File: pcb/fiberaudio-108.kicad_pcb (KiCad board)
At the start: 2 copper layers, 0 parts

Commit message: Add schematic, custom components and initial layout
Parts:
- added C1: 10nF, Capacitor_SMD:C_0805_2012Metric, F.Cu at (68.6, 42.2)
- added C2: 100nF, Capacitor_SMD:C_0805_2012Metric, F.Cu at (73.7, 41.9)
- added C3: 4.7uF, Capacitor_Tantalum_SMD:CP_EIA-3216-18_Kemet-A, F.Cu at (76.2, 42.0)
- added C4: 4.7uF, Capacitor_SMD:C_0805_2012Metric, F.Cu at (78.7, 58.4)
- added C5: 20pF, Capacitor_SMD:C_0805_2012Metric, F.Cu at (94.0, 58.4)
- added C6: 20pF, Capacitor_SMD:C_0805_2012Metric, F.Cu at (86.4, 58.4)
- added C7: 100nF, Capacitor_SMD:C_0805_2012Metric, F.Cu at (81.3, 58.4)
- added C8: 4.7uF, Capacitor_SMD:C_0805_2012Metric, F.Cu at (86.4, 41.9)
- added C9: 100nF, Capacitor_SMD:C_0805_2012Metric, F.Cu at (107.6, 45.7)
- added FB1: 33R@100MHz, Inductor_SMD:L_0805_2012Metric, F.Cu at (71.1, 45.7)
- added J1: USB_B_Mini, Connector_USB:USB_Mini-B_Lumberg_2486_01_Horizontal, F.Cu at (62.2, 49.5)
- added J2: PLT133_T10W, custom:PLT133_T10W, F.Cu at (115.6, 49.5)
- added LD1: rd, LED_THT:LED_D3.0mm_FlatTop, F.Cu at (100.3, 49.5)
- added Q1: DMG2301L, Package_TO_SOT_SMD:SOT-23, F.Cu at (108.0, 49.5)
- added R1: 270, Resistor_SMD:R_0805_2012Metric, F.Cu at (101.6, 53.3)
- added R2: 560, Resistor_SMD:R_0805_2012Metric, F.Cu at (108.0, 53.3)
- added SW1: MUTE, Button_Switch_SMD:SW_SPST_B3S-1000, F.Cu at (94.0, 49.5)
- added U1: STF202-22T1, Package_SO:TSOP-6_1.65x3.05mm_P0.95mm, F.Cu at (71.1, 49.5)
- added U2: AT93C46E, Package_SO:SOIC-8_3.9x4.9mm_P1.27mm, F.Cu at (71.1, 55.9)
- added U3: CM108AH, Package_QFP:LQFP-48_7x7mm_P0.5mm, F.Cu at (82.5, 49.5)
- added Y1: 12MHz, Crystal:Crystal_SMD_3225-4Pin_3.2x2.5mm, F.Cu at (90.2, 58.4)

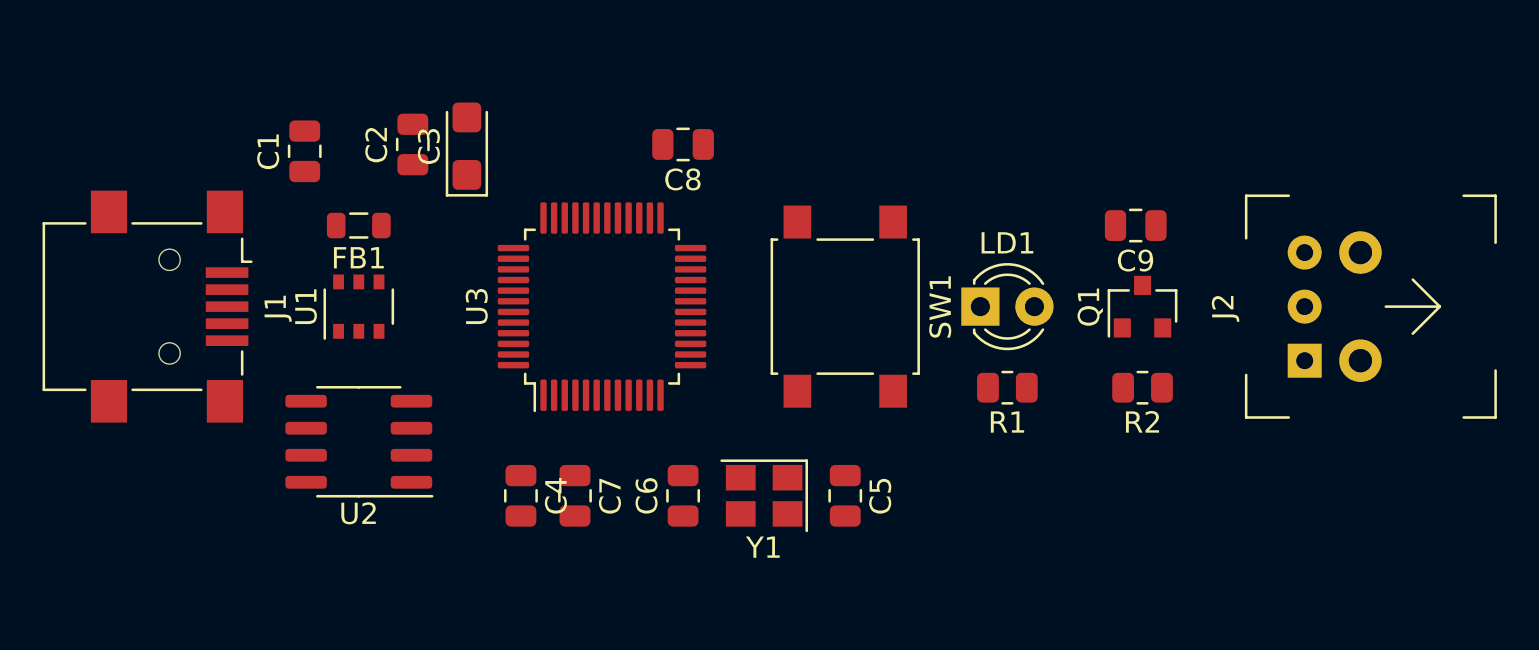
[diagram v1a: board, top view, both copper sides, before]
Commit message: Add initial routed layout
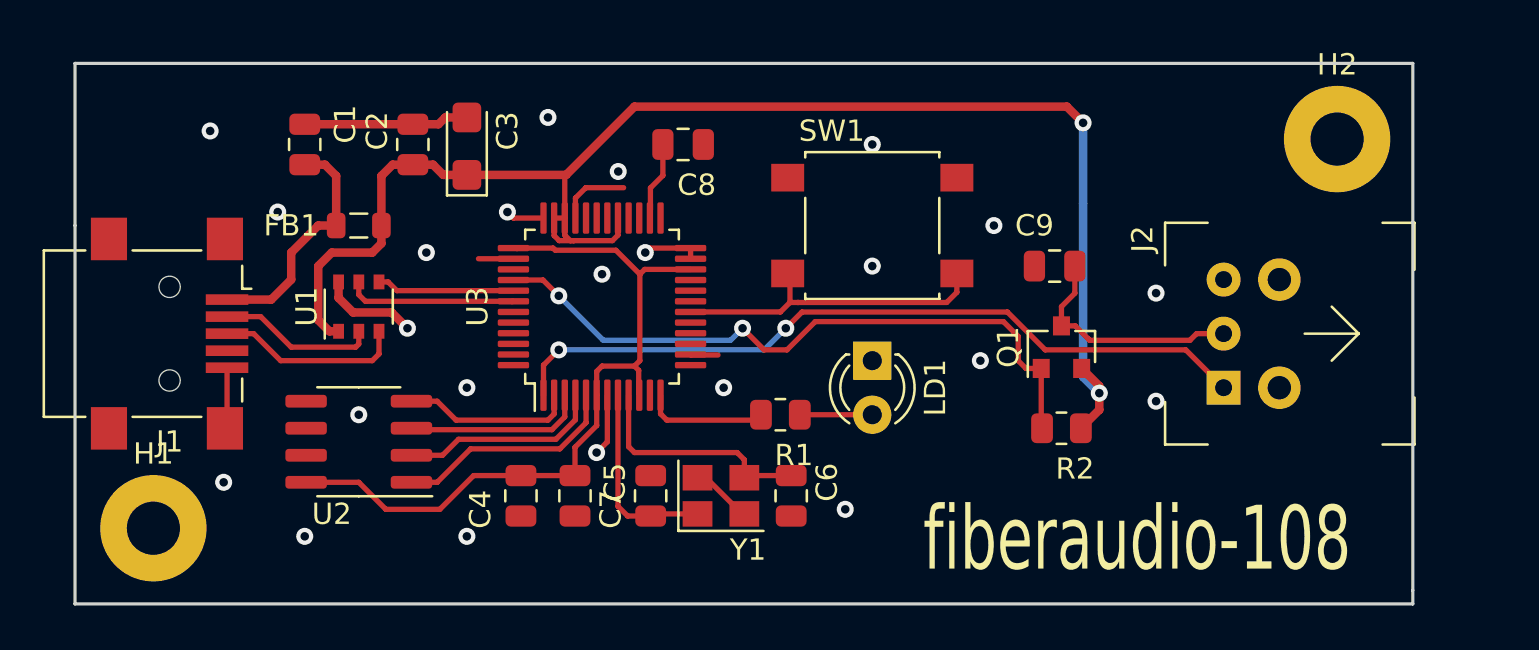
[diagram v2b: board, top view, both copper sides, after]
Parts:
- added H1: MountingHole_Pad, MountingHole:MountingHole_2.5mm_Pad, F.Cu at (61.5, 59.9)
- added H2: MountingHole_Pad, MountingHole:MountingHole_2.5mm_Pad, F.Cu at (117.1, 41.7)
- moved R1 10.7 mm to (90.9, 54.6)
- moved C5 9.14 mm to (84.8, 58.4), turned to 90 degrees
- moved LD1 5.68 mm to (95.2, 52.1), turned to 270 degrees
- moved C6 5.08 mm to (91.4, 58.4), turned to 270 degrees
- moved C9 4.26 mm to (103.8, 47.6)
- moved Q1 4.26 mm to (104.1, 51.4)
- moved R2 4.26 mm to (104.1, 55.2)
- moved SW1 4.02 mm to (95.2, 45.7), turned to 0 degrees
- moved J2 4.02 mm to (111.8, 50.8)
- moved Y1 2.03 mm to (88.1, 58.4), turned to 0 degrees
- moved J1 1.27 mm to (62.2, 50.8)
- moved C1 0.32 mm to (68.6, 41.9)
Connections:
- U3 pad 6: Net-(U3-Pad6) -> +3V3
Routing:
- net +5V: track 0.21 -> 70.6 mm, vias 0 -> 2
- net +3V3: track 0.00 -> 36.0 mm
- net /SPDIF_MOD: track 0.00 -> 35.9 mm, vias 0 -> 2
- net GND: track 0.00 -> 31.9 mm, vias 0 -> 23
- net /SPDIF_PWDN: track 0.00 -> 31.6 mm, vias 0 -> 2
- net /MUTE: track 0.00 -> 15.2 mm
- net /EECS: track 0.00 -> 11.5 mm
- net /VBUS: track 0.00 -> 11.3 mm
- net Net-(C9-Pad1): track 0.00 -> 11.1 mm
- net Net-(C6-Pad1): track 0.00 -> 10.7 mm
- net /EESK: track 0.00 -> 9.55 mm
- net Net-(C5-Pad1): track 0.00 -> 9.19 mm
- net /USBDP: track 0.00 -> 8.86 mm
- net /EEMOSI: track 0.00 -> 8.50 mm
- net /EEMISO: track 0.00 -> 8.07 mm
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- added copper zone on B.Cu, net GND
- added copper zone on F.Cu, net GND
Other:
- board outline added: 62.9 x 25.4 mm
- board text added: "fiberaudio-108"

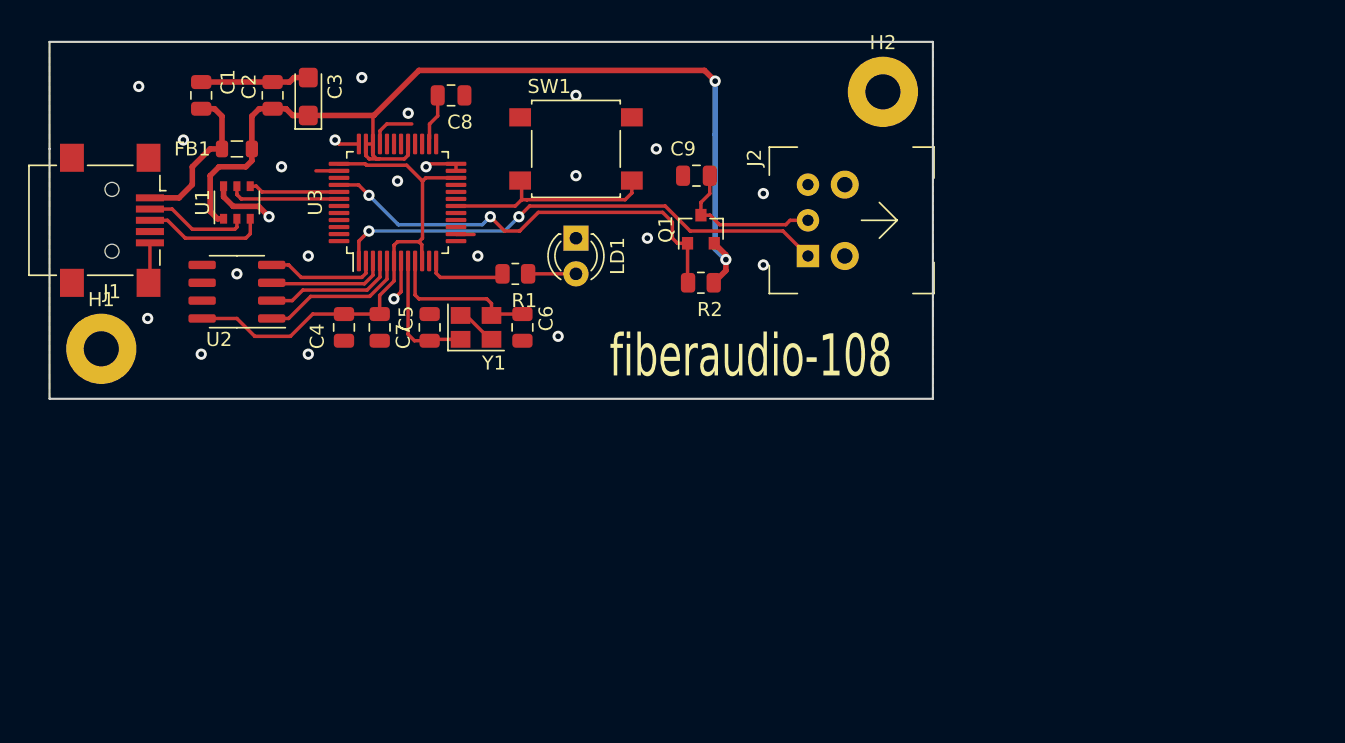
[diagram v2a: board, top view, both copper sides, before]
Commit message: Redesign for automated assembly
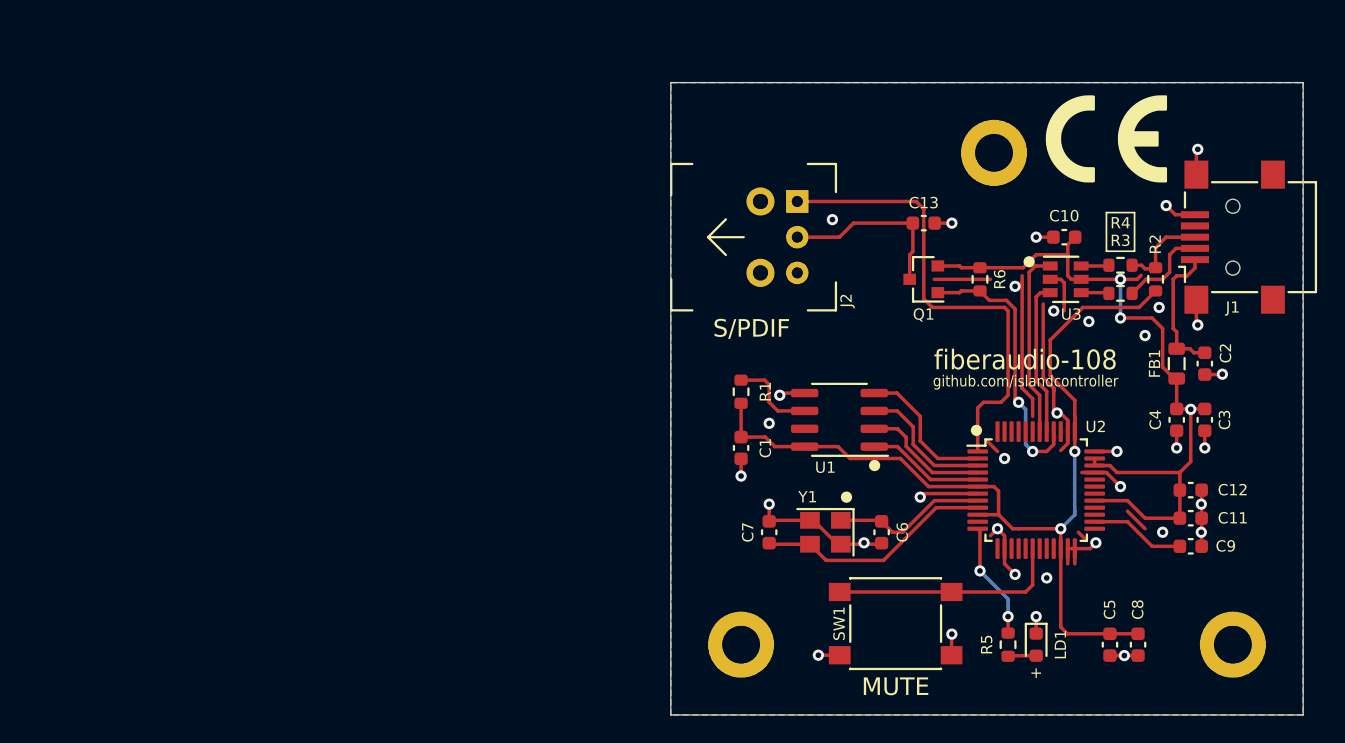
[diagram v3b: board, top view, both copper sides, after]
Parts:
- added C10: 100nF, Capacitor_SMD:C_0603_1608Metric, F.Cu at (130.0, 52.0)
- added C11: 100nF, Capacitor_SMD:C_0603_1608Metric, F.Cu at (139.0, 72.0)
- added C12: 100nF, Capacitor_SMD:C_0603_1608Metric, F.Cu at (139.0, 70.0)
- added C13: 100nF, Capacitor_SMD:C_0603_1608Metric, F.Cu at (120.0, 51.0)
- added H3: MountingHole_Pad, MountingHole:MountingHole_2.7mm_M2.5_DIN965_Pad, F.Cu at (125.0, 46.0)
- added R3: 22, Resistor_SMD:R_0603_1608Metric, F.Cu at (134.0, 56.0)
- added R4: 22, Resistor_SMD:R_0603_1608Metric, F.Cu at (134.0, 54.0)
- added R5: 330, Resistor_SMD:R_0603_1608Metric, F.Cu at (126.0, 81.0)
- added R6: 560, Resistor_SMD:R_0603_1608Metric, F.Cu at (124.0, 55.0)
- added REF**: CE-Logo_8.5x6mm_SilkScreen, Symbol:CE-Logo_8.5x6mm_SilkScreen, F.Cu at (133.0, 45.0)
- C1: value 10nF -> 100nF; footprint Capacitor_SMD:C_0805_2012Metric -> Capacitor_SMD:C_0603_1608Metric
- C2: value 100nF -> 10nF; footprint Capacitor_SMD:C_0805_2012Metric -> Capacitor_SMD:C_0603_1608Metric
- C3: value 4.7uF -> 100nF; footprint Capacitor_Tantalum_SMD:CP_EIA-3216-18_Kemet-A -> Capacitor_SMD:C_0603_1608Metric
- C4, C6: footprint Capacitor_SMD:C_0805_2012Metric -> Capacitor_SMD:C_0603_1608Metric
- C5: value 20pF -> 4.7uF; footprint Capacitor_SMD:C_0805_2012Metric -> Capacitor_SMD:C_0603_1608Metric
- C7: value 100nF -> 20pF; footprint Capacitor_SMD:C_0805_2012Metric -> Capacitor_SMD:C_0603_1608Metric
- C8: value 4.7uF -> 100nF; footprint Capacitor_SMD:C_0805_2012Metric -> Capacitor_SMD:C_0603_1608Metric
- C9: value 100nF -> 4.7uF; footprint Capacitor_SMD:C_0805_2012Metric -> Capacitor_SMD:C_0603_1608Metric
- FB1: value 33R@100MHz -> 100R@100MHz
- H1, H2: footprint MountingHole:MountingHole_2.5mm_Pad -> MountingHole:MountingHole_2.7mm_M2.5_DIN965_Pad
- LD1: footprint LED_THT:LED_D3.0mm_FlatTop -> LED_SMD:LED_0603_1608Metric
- Q1: value DMG2301L -> SI2301CDS
- R1: value 270 -> 0; footprint Resistor_SMD:R_0805_2012Metric -> Resistor_SMD:R_0603_1608Metric
- R2: value 560 -> 1k5; footprint Resistor_SMD:R_0805_2012Metric -> Resistor_SMD:R_0603_1608Metric
- SW1: footprint Button_Switch_SMD:SW_SPST_B3S-1000 -> Button_Switch_SMD:SW_SPST_PTS645
- U1: value STF202-22T1 -> AT93C46D; footprint Package_SO:TSOP-6_1.65x3.05mm_P0.95mm -> Package_SO:SOIC-8_3.9x4.9mm_P1.27mm
- U2: value AT93C46E -> CM108AH; footprint Package_SO:SOIC-8_3.9x4.9mm_P1.27mm -> Package_QFP:LQFP-48_7x7mm_P0.5mm
- U3: value CM108AH -> SRV05-4; footprint Package_QFP:LQFP-48_7x7mm_P0.5mm -> Package_TO_SOT_SMD:SOT-23-6
- moved H1 83.2 mm to (142.0, 81.0)
- moved J1 79.8 mm to (142.0, 52.0), turned to 90 degrees
- moved C2 69.0 mm to (140.0, 61.0), turned to 270 degrees
- moved FB1 68.6 mm to (138.0, 61.0), turned to 90 degrees
- moved C3 67.8 mm to (140.0, 65.0), turned to 270 degrees
- moved C8 62.6 mm to (135.2, 81.0), turned to 270 degrees
- moved C4 59.6 mm to (138.0, 65.0)
- moved U2 58.6 mm to (128.0, 70.0), turned to 0 degrees
- moved C5 53.4 mm to (133.2, 81.0), turned to 270 degrees
- moved U3 47.9 mm to (130.1, 55.0), turned to 0 degrees
- moved C1 45.9 mm to (107.0, 67.0), turned to 270 degrees
- moved U1 45.6 mm to (114.0, 65.0), turned to 180 degrees
- moved C9 44.0 mm to (139.0, 74.0), turned to 0 degrees
- moved LD1 43.7 mm to (128.0, 81.0)
- moved SW1 40.7 mm to (118.0, 79.5), turned to 180 degrees
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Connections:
- C1 pad 1: /VBUS -> +3V3
- C2 pad 1: +5V -> /VBUS
- C4 pad 1: +3V3 -> +5V
- C5 pad 1: Net-(C5-Pad1) -> +3V3
- C7 pad 1: +3V3 -> Net-(C7-Pad1)
- C8 pad 1: GND -> +3V3
- C8 pad 2: Net-(C8-Pad2) -> GND
- J1 pad 2: /USBDN -> /USBD_IN_N
- J1 pad 3: /USBDP -> /USBD_IN_P
- J2 pad 2: Net-(C9-Pad1) -> Net-(C13-Pad1)
- Q1 pad 3: Net-(C9-Pad1) -> Net-(C13-Pad1)
- R1 pad 1: Net-(LD1-Pad2) -> +3V3
- R2 pad 1: +5V -> +3V3
- R2 pad 2: /SPDIF_PWDN -> /USBD_IN_P
- U1 pad 1: +5V -> /EECS
- U1 pad 2: /USBDN -> /EESK
- U1 pad 3: /USBDP -> /EEMOSI
- U1 pad 4: /USBDP_C -> /EEMISO
- U1 pad 5: /USBDN_C -> GND
- U1 pad 6: GND -> Net-(R1-Pad2)
- U2 pad 1: /EECS -> /SPDIF_MOD
- U2 pad 2: /EESK -> /EEMISO
- U2 pad 4: /EEMISO -> /EESK
- U2 pad 5: GND -> /EECS
- U2 pad 6: Net-(U2-Pad6) -> +3V3
- U2 pad 7: Net-(U2-Pad7) -> GND
- U2 pad 8: +3V3 -> Net-(C6-Pad1)
- U3 pad 1: /SPDIF_MOD -> /USBD_N
- U3 pad 2: /EEMISO -> GND
- U3 pad 3: /EEMOSI -> /USBD_P
- U3 pad 4: /EESK -> /USBD_R_N
- U3 pad 5: /EECS -> +5V
- U3 pad 6: +3V3 -> /USBD_R_P
- Y1 pad 1: Net-(C5-Pad1) -> Net-(C6-Pad1)
- Y1 pad 3: Net-(C6-Pad1) -> Net-(C7-Pad1)
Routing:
- net GND: track 31.9 -> 86.6 mm, vias 23 -> 35
- net +3V3: track 36.0 -> 66.8 mm, vias 0 -> 2
- net Net-(C7-Pad1): track 0.00 -> 17.1 mm
- net +5V: track 70.6 -> 53.9 mm, vias 2 -> 3
- net /USBD_N: track 0.00 -> 13.3 mm
- net Net-(C13-Pad1): track 0.00 -> 12.7 mm
- net /SPDIF_PWDN: track 31.6 -> 19.6 mm
- net /USBD_P: track 0.00 -> 11.0 mm
- net Net-(C5-Pad1): track 9.19 -> 0.00 mm
- net /USBDP: track 8.86 -> 0.00 mm
- net /LEDO: track 0.00 -> 8.32 mm, vias 0 -> 2
- net /USBDN_C: track 8.06 -> 0.00 mm
- net /USBDN: track 7.44 -> 0.00 mm
- net /USBD_IN_N: track 0.00 -> 6.53 mm
- net /USBDP_C: track 6.49 -> 0.00 mm
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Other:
- board size 62.9 x 25.4 mm -> 45 x 45 mm
- rule trace_min: 0.2 -> 0.25
- rule via_min_drill: 0.3 -> 0.35
- rule via_min_size: 0.4 -> 0.8
- board text added: "+"
- board text added: "MUTE"
- board text added: "S/PDIF"
- board text added: "github.com/islandcontroller"

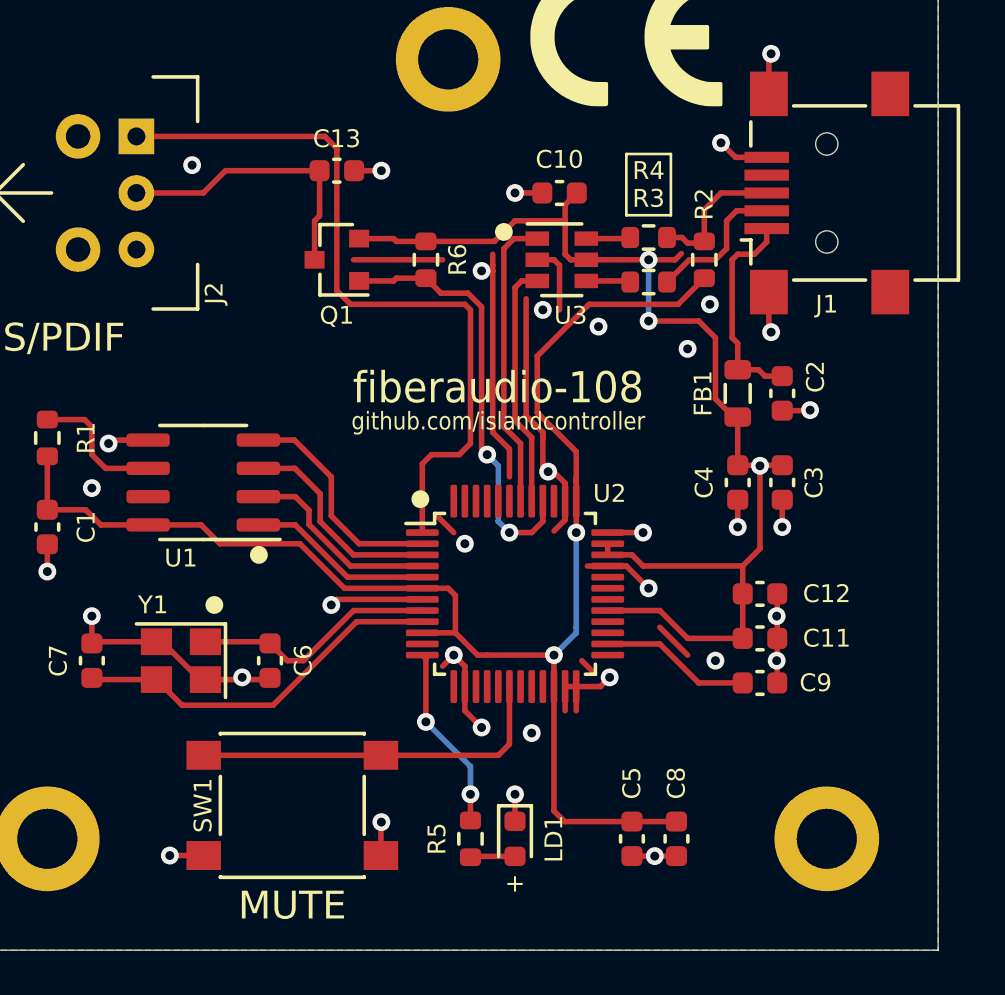
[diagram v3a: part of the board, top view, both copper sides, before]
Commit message: Added testpoints; Removed erroneous file
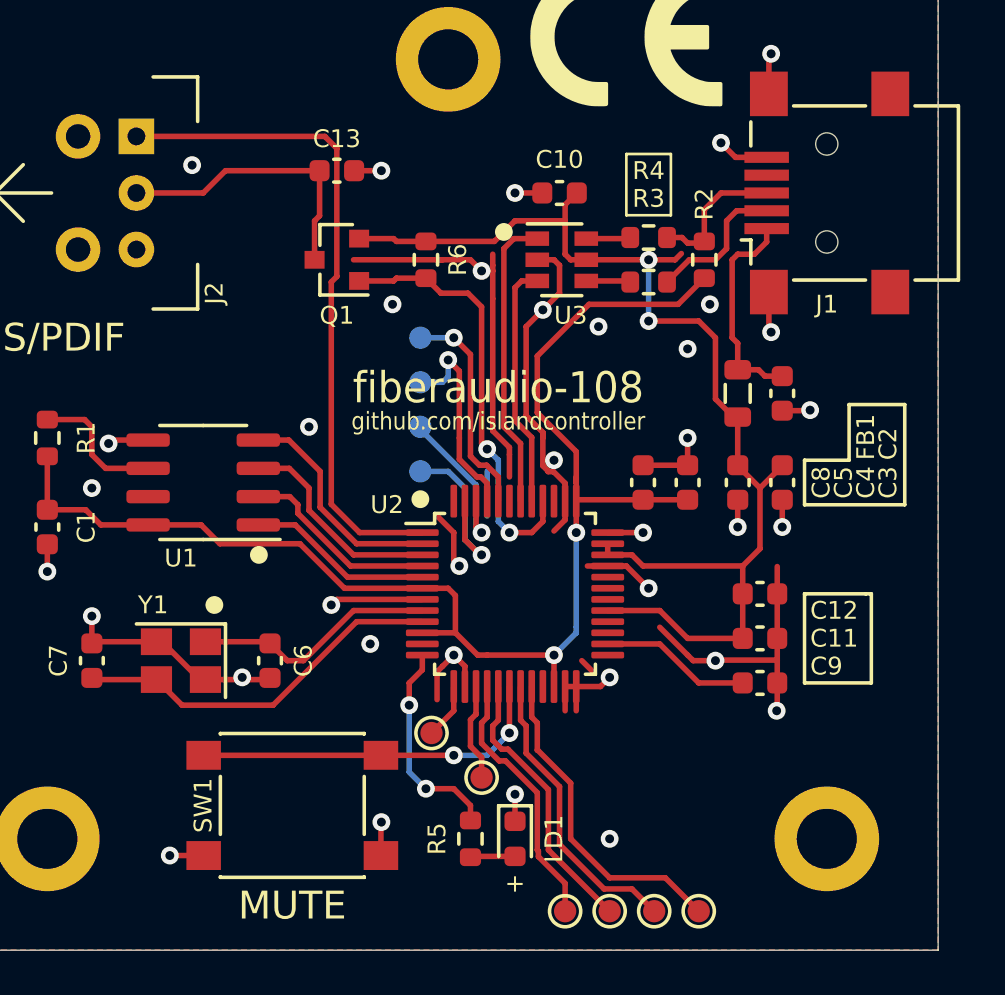
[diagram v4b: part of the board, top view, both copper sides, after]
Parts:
- added TP1: SDIN, TestPoint:TestPoint_Pad_D1.0mm, F.Cu at (130.2, 84.2)
- added TP10: GPIO4, TestPoint:TestPoint_Pad_D1.0mm, F.Cu at (126.5, 78.2)
- added TP2: ADSCLK, TestPoint:TestPoint_Pad_D1.0mm, F.Cu at (132.2, 84.2)
- added TP3: ADLRCK, TestPoint:TestPoint_Pad_D1.0mm, F.Cu at (134.2, 84.2)
- added TP4: ADMCLK, TestPoint:TestPoint_Pad_D1.0mm, F.Cu at (136.2, 84.2)
- added TP5: SDOUT, TestPoint:TestPoint_Pad_D1.0mm, B.Cu at (123.8, 58.5)
- added TP6: DAMCLK, TestPoint:TestPoint_Pad_D1.0mm, B.Cu at (123.8, 60.5)
- added TP7: DALRCK, TestPoint:TestPoint_Pad_D1.0mm, B.Cu at (123.8, 62.5)
- added TP9: GPIO3, TestPoint:TestPoint_Pad_D1.0mm, F.Cu at (124.2, 76.2)
- added TPe: DASCLK, TestPoint:TestPoint_Pad_D1.0mm, B.Cu at (123.8, 64.5)
- moved C5 16.2 mm to (135.8, 65.0), turned to 90 degrees
- moved C8 16.1 mm to (133.8, 65.0), turned to 90 degrees
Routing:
- net Net-(TP4-Pad1): track 0.00 -> 14.7 mm
- net Net-(TP3-Pad1): track 0.00 -> 13.3 mm
- net GND: track 86.6 -> 99.7 mm, vias 35 -> 36
- net Net-(TP2-Pad1): track 0.00 -> 12.5 mm
- net Net-(TP1-Pad1): track 0.00 -> 11.9 mm
- net Net-(TP5-Pad1): track 0.00 -> 9.86 mm, vias 0 -> 1
- net Net-(TP6-Pad1): track 0.00 -> 9.27 mm, vias 0 -> 1
- net Net-(TP8-Pad1): track 0.00 -> 8.43 mm, vias 0 -> 1
- net Net-(TP7-Pad1): track 0.00 -> 7.41 mm, vias 0 -> 1
- net +3V3: track 66.8 -> 60.5 mm
- net Net-(TP10-Pad1): track 0.00 -> 4.40 mm
- net /SPDIF_MOD: track 33.6 -> 29.9 mm
- net Net-(TP9-Pad1): track 0.00 -> 2.50 mm
- net /LEDO: track 8.32 -> 9.54 mm
- net /EEMISO: track 10.3 -> 11.0 mm
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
